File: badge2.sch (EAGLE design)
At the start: 322 parts, among them IC1 LPC4330FET180, IC14 AT45DB041D, IC15 MCP73833, IC17 MAX15101EWL, IC18 MAX15101EWL, IC4 74AC04D, IC6 MAX2837ETM+, J2 U.FL, SW2 JS102011SAQN, X2 MICROUSB, X3 NOKIA

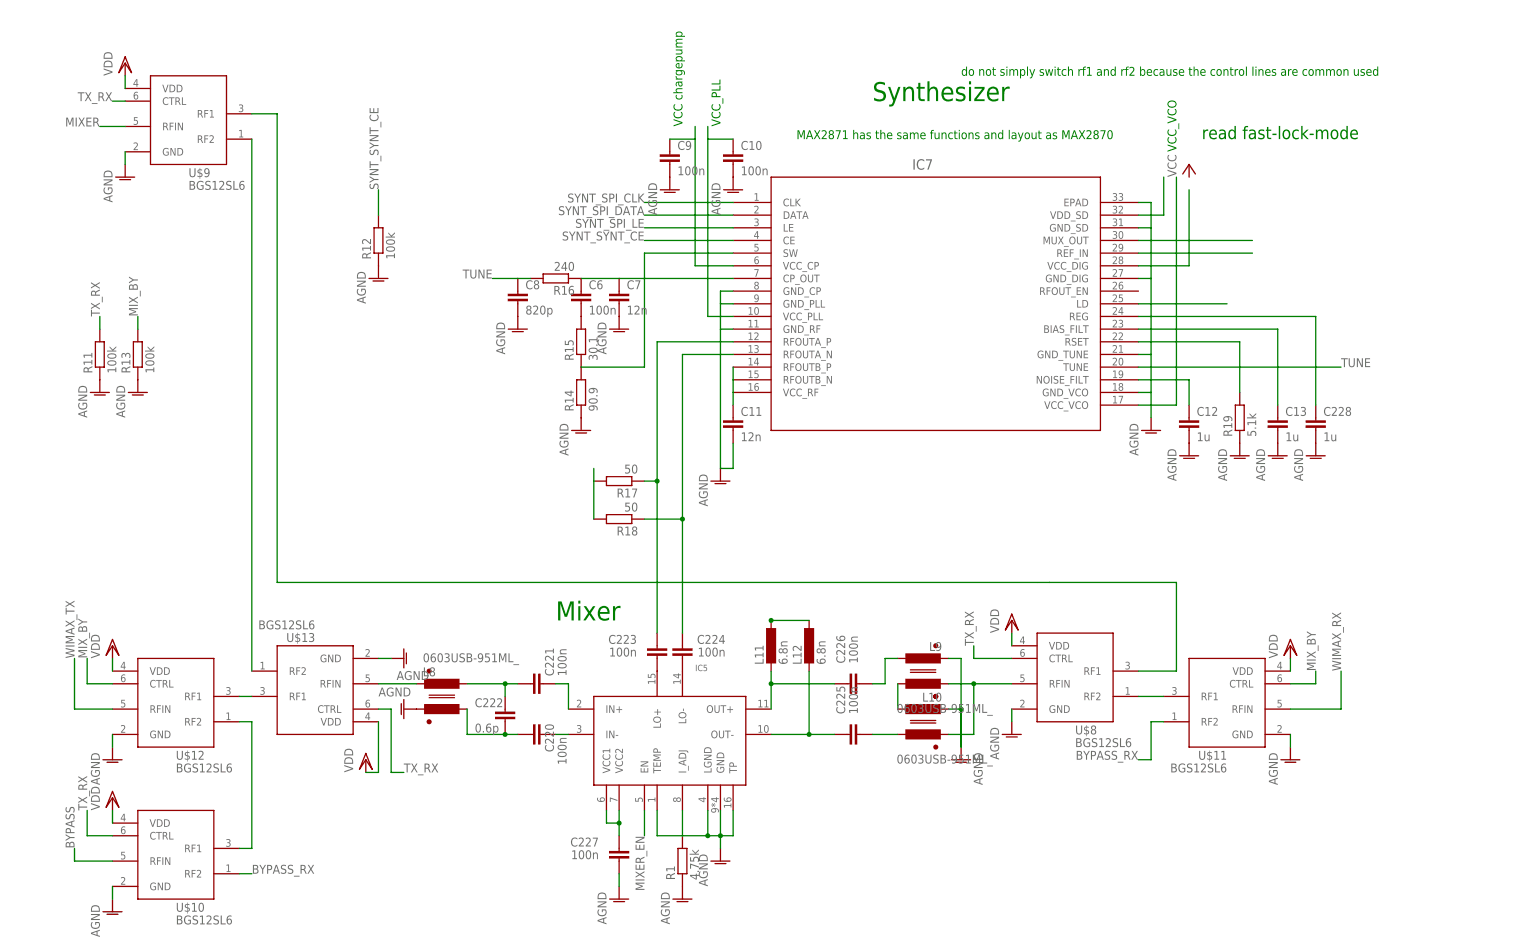
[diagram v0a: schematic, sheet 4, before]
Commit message: Start with the RF-Layout
Place the components and change the rf-switches to get a good route
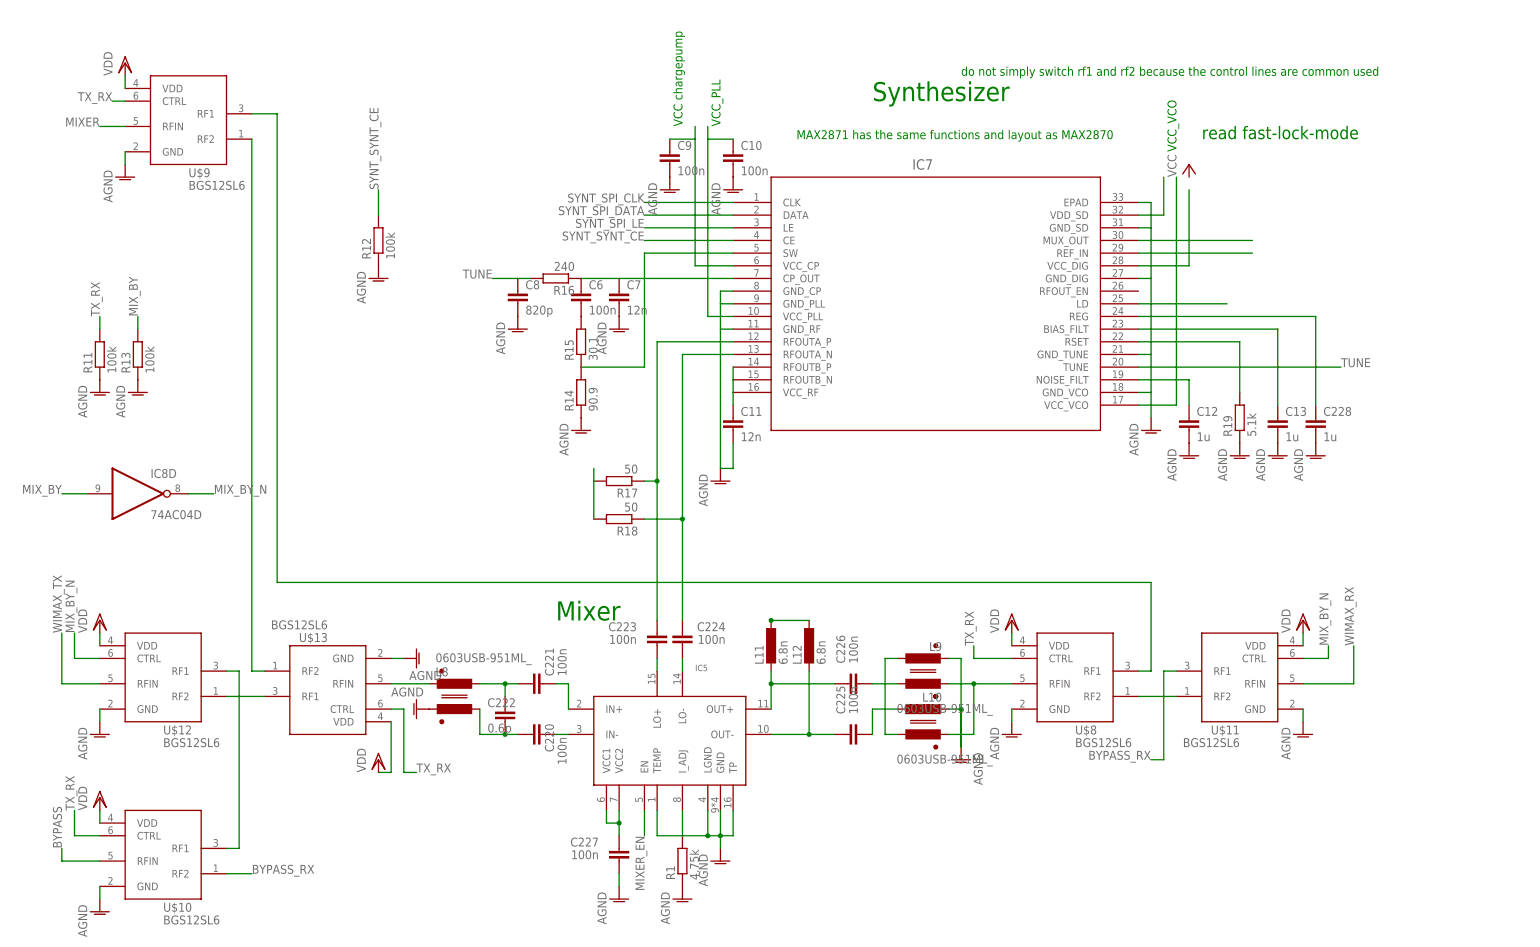
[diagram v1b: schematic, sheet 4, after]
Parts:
- added IC8: 74AC04D, 74xx-eu:74AC04D
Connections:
- new net LOW_HIGH_FILT_N: IC4C.O, U$7.CTRL
- new net MIX_BY_N: IC8D.O, U$11.CTRL, U$12.CTRL
- net AGND: now also U$13.GND
- net BYPASS_RX: now also U$11.RF1; no longer U$11.RF2
- net LOW_HIGH_FILT: now also IC4C.I; no longer U$7.CTRL
- net MIX_BY: now also IC8D.I; no longer U$11.CTRL, U$12.CTRL
- net N$10: now also FL2.OUT; no longer FL1.OUT
- net N$104: now also C225.1; no longer L9.4
- net N$109: now also L9.1; no longer C225.1
- net N$11: now also U$12.RF2; no longer U$12.RF1
- net N$110: now also L9.4; no longer L9.1
- net N$16: now also U$11.RF2; no longer U$11.RF1
- net N$4: now also U$12.RF1; no longer U$12.RF2
- net N$9: now also FL1.OUT; no longer FL2.OUT
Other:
- moved on the sheet: C223, C224, IC4C, L8, U$10, U$11, U$12, U$13, U$7
